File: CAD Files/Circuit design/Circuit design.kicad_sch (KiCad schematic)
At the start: 8 parts, among them J1 Conn_01x07_Socket, J2 Conn_01x07_Socket, J3 Pin to Electrode

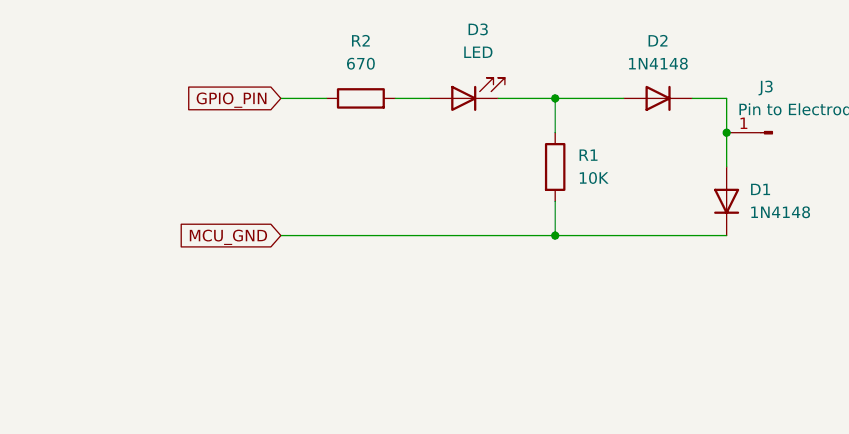
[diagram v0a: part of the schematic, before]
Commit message: Added to ReadME and added more photos
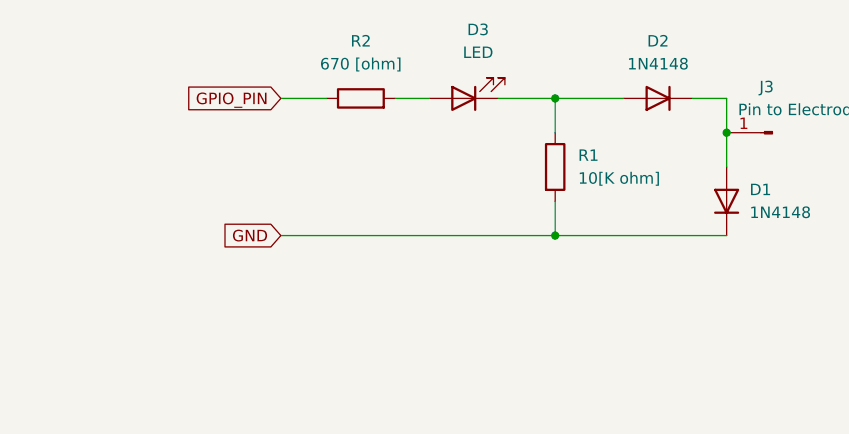
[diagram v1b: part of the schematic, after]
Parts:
- R1: value 10K -> 10[K ohm]
- R2: value 670 -> 670 [ohm]
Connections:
- net MCU_GND: no longer D1.1 (K), R1.2
- new net GND: D1.1 (K), R1.2
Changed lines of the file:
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@@
 		)
 	)
-	(global_label "MCU_GND"
+	(global_label "GND"
 		(shape input)
 		(at 182.88 53.34 180)
@@
 		)
 		(property "Intersheetrefs" "${INTERSHEET_REFS}"
-			(at 171.0048 53.34 0)
+			(at 176.0243 53.34 0)
 			(effects
 				(font
@@
 			)
 		)
-		(property "Value" "10K"
+		(property "Value" "10[K ohm]"
 			(at 215.9 46.9899 0)
 			(effects
@@
 			)
 		)
-		(property "Value" "670"
+		(property "Value" "670 [ohm]"
 			(at 191.77 34.29 90)
 			(effects
